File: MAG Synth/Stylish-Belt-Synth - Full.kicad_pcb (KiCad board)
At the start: 2 copper layers, 177.8 x 101.7 mm, 75 parts, among them J0 USB_B, J1 Headphone, J26 WRITE PATCH, J27 PARAM SELECT, J28 PATCH SELECT, J29 MODE, J30 STYLUS, U1 stm32f103c8t6-module-china, U2 XPT8871

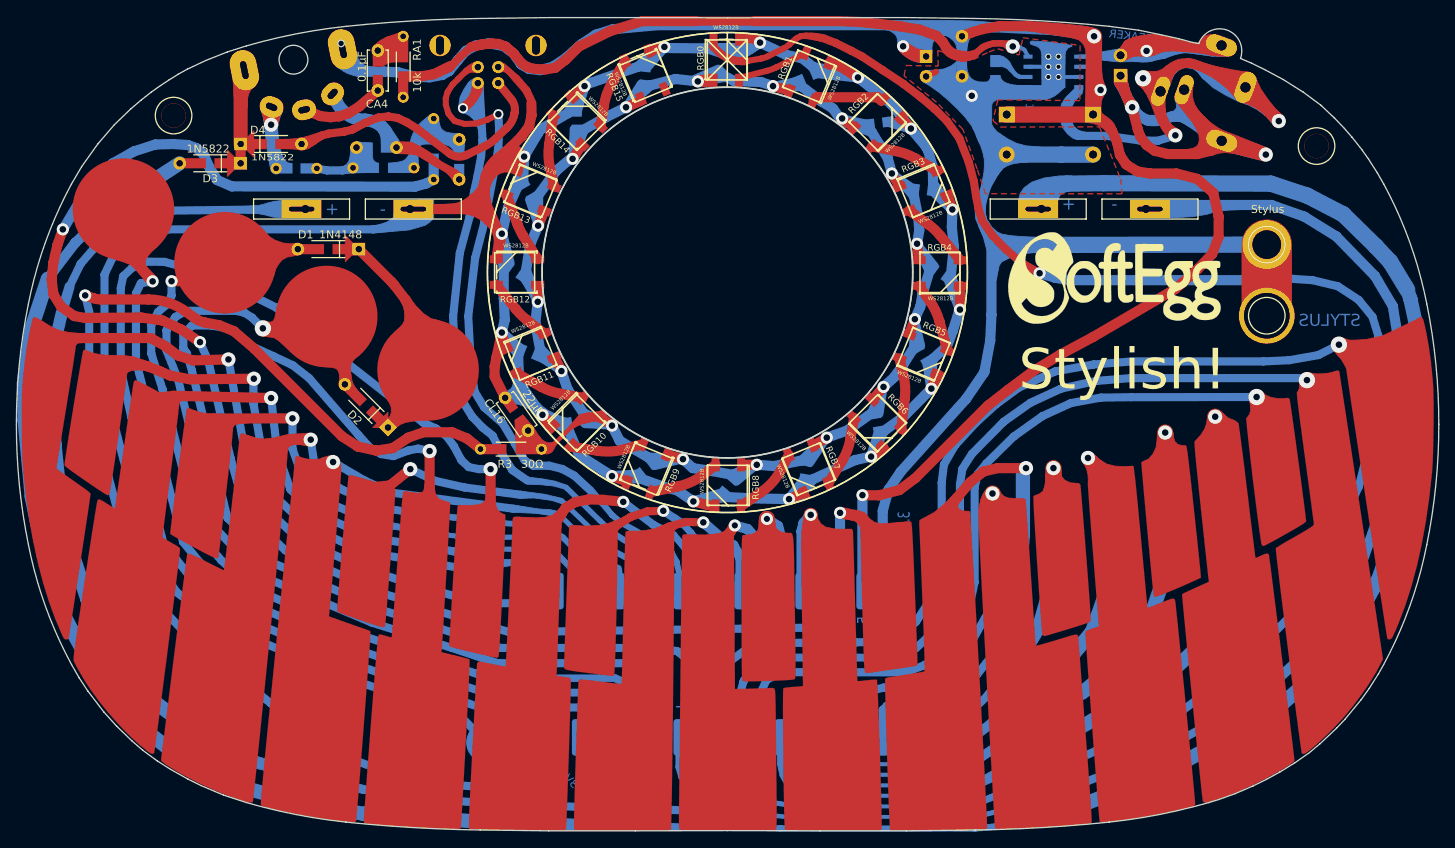
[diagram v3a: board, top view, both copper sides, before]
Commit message: Special "3d print only" parts with thickened details that might not be injection mold friendly. Update on the PCB. Blue pill 3d model Updated Volume Wheel.
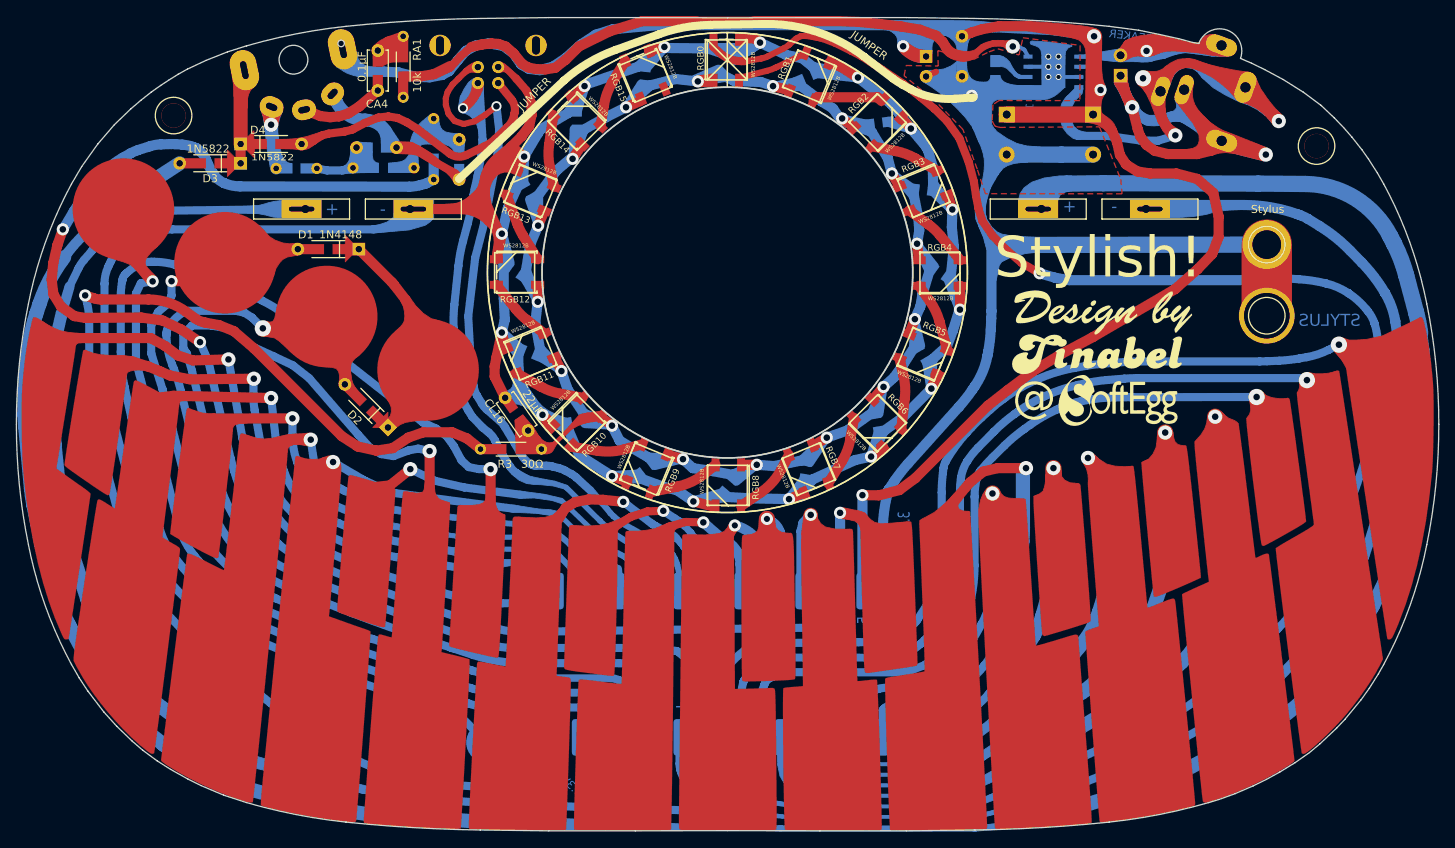
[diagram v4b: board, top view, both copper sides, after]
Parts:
- removed the ~ at (196.8, 86.7)
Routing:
- net Net-(BT34H1-+): track 341.8 -> 344.7 mm
- net Net-(J0-D+): track 89.7 -> 90.8 mm
- net /PARAM: track 122.5 -> 121.5 mm
- net Net-(J0-D-): track 86.1 -> 86.8 mm
- net /AUDIO_OUT: track 182.8 -> 182.3 mm
- added copper zone on F.Cu, net GND
- removed copper zone on F.Cu, net +5V
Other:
- board text added: "+5V"
- board text added: "@"
- board text added: "A#0"
- board text added: "A#1"
- board text added: "A0"
- board text added: "A1"
- board text added: "B#1"
- board text added: "B0"
- board text added: "C#0"
- board text added: "C#1"
- board text added: "C0"
- board text added: "C1"
- board text added: "C2"
- board text added: "D#0"
- board text added: "D#1"
- board text added: "D+"
- board text added: "D-"
- board text added: "D0"
- board text added: "D1"
- board text added: "E0"
- board text added: "E1"
- board text added: "F#0"
- board text added: "F#1"
- board text added: "F0"
- board text added: "F1"
- board text added: "G#0"
- board text added: "G#1"
- board text added: "G0"
- board text added: "G1"
- board text added: "GND"
- board text added: "JUMPER"
- board text added: "LED"
- board text added: "PARAM"
- board text added: "PATCH"
- board text added: "WRITE"
